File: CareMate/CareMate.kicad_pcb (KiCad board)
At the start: 2 copper layers, 88.9 x 76.2 mm, 24 parts, among them J1 Barrel_Jack_MountingPin, J2 Conn_01x16, J3 Conn_01x03, J4 Conn_01x03, J5 Conn_01x06, J6 Conn_01x03, J7 Servo, J9 Conn_01x16, U1 L7805, U2 LM386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

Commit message: fixed unconnected items
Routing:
- net GND: track 9.79 -> 35.2 mm, vias 1 -> 7
- added copper zone on B.Cu, net GND
- removed copper zone on B.Cu, net (none)
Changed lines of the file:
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@@
     (thickness 1.6)
     (drawings 10)
-    (tracks 240)
+    (tracks 258)
     (zones 0)
     (modules 24)
@@
   )
   (setup
-    (last_trace_width 0.381)
+    (last_trace_width 0.635)
     (user_trace_width 0.254)
     (user_trace_width 0.381)
@@
     (solder_mask_min_width 0.25)
     (aux_axis_origin 0 0)
-    (visible_elements 7FFFF7FF)
+    (visible_elements 7FFFFFFF)
     (pcbplotparams
       (layerselection 0x010fc_ffffffff)
@@
   (segment (start 123.952 27.686) (end 124.46 27.178) (width 0.381) (layer F.Cu) (net 2))
   (segment (start 122.654 27.686) (end 123.952 27.686) (width 0.381) (layer F.Cu) (net 2))
+  (via (at 113.284 52.324) (size 0.8) (drill 0.4) (layers F.Cu B.Cu) (net 2))
+  (segment (start 111.252 51.308) (end 112.268 51.308) (width 0.25) (layer F.Cu) (net 2))
+  (segment (start 112.268 51.308) (end 113.284 52.324) (width 0.25) (layer F.Cu) (net 2))
+  (segment (start 111.873 53.735) (end 113.284 52.324) (width 0.25) (layer F.Cu) (net 2))
+  (segment (start 111.252 53.735) (end 111.873 53.735) (width 0.25) (layer F.Cu) (net 2))
+  (via (at 98.552 33.782) (size 0.8) (drill 0.4) (layers F.Cu B.Cu) (net 2))
+  (segment (start 106.172 33.878) (end 98.648 33.878) (width 0.25) (layer F.Cu) (net 2))
+  (segment (start 98.648 33.878) (end 98.552 33.782) (width 0.25) (layer F.Cu) (net 2))
+  (via (at 62.484 41.402) (size 0.8) (drill 0.4) (layers F.Cu B.Cu) (net 2))
+  (segment (start 57.59 41.42) (end 62.466 41.42) (width 0.25) (layer F.Cu) (net 2))
+  (segment (start 62.466 41.42) (end 62.484 41.402) (width 0.25) (layer F.Cu) (net 2))
+  (via (at 54.102 67.056) (size 0.8) (drill 0.4) (layers F.Cu B.Cu) (net 2))
+  (segment (start 54.102 67.08) (end 54.102 67.056) (width 0.25) (layer B.Cu) (net 2))
+  (segment (start 50.292 70.89) (end 54.102 67.08) (width 0.25) (layer B.Cu) (net 2))
+  (via (at 133.096 39.624) (size 0.8) (drill 0.4) (layers F.Cu B.Cu) (net 2))
+  (via (at 134.112 44.704) (size 0.8) (drill 0.4) (layers F.Cu B.Cu) (net 2))
+  (segment (start 133.374 43.966) (end 134.112 44.704) (width 0.635) (layer B.Cu) (net 2))
+  (segment (start 132.08 43.966) (end 133.374 43.966) (width 0.635) (layer B.Cu) (net 2))
   (segment (start 111.111 55.626) (end 111.252 55.485) (width 0.381) (layer F.Cu) (net 3))
   (segment (start 106.172 55.626) (end 111.111 55.626) (width 0.381) (layer F.Cu) (net 3))
@@
   (segment (start 93.016 76.962) (end 92.964 77.014) (width 0.381) (layer F.Cu) (net 13))
   (segment (start 99.06 76.962) (end 93.016 76.962) (width 0.381) (layer F.Cu) (net 13))
-  (segment (start 67.362 51.816) (end 67.564 51.614) (width 0.381) (layer F.Cu) (net 22))
   (via (at 89.916 54.356) (size 0.8) (drill 0.4) (layers F.Cu B.Cu) (net 14))
   (segment (start 92.646 92.27) (end 89.916 89.54) (width 0.381) (layer B.Cu) (net 14))
@@
   (segment (start 66.899658 68.326) (end 67.201157 68.024501) (width 0.381) (layer F.Cu) (net 21))
   (segment (start 64.77 68.326) (end 66.899658 68.326) (width 0.381) (layer F.Cu) (net 21))
+  (segment (start 67.362 51.816) (end 67.564 51.614) (width 0.381) (layer F.Cu) (net 22))
   (via (at 50.038 52.07) (size 0.8) (drill 0.4) (layers F.Cu B.Cu) (net 22))
   (segment (start 67.564 51.614) (end 50.494 51.614) (width 0.381) (layer F.Cu) (net 22))
@@
   (segment (start 59.499188 49.82) (end 59.923689 50.244501) (width 0.381) (layer F.Cu) (net 37))
   (segment (start 57.59 49.82) (end 59.499188 49.82) (width 0.381) (layer F.Cu) (net 37))
-  (zone (net 0) (net_name "") (layer B.Cu) (hatch edge 0.508)
-    (connect_pads yes (clearance 0.508))
+  (zone (net 2) (net_name GND) (layer B.Cu) (hatch edge 0.508)
+    (connect_pads (clearance 0.508))
     (min_thickness 0.254)
     (fill yes (arc_segments 32) (thermal_gap 0.508) (thermal_bridge_width 0.508))

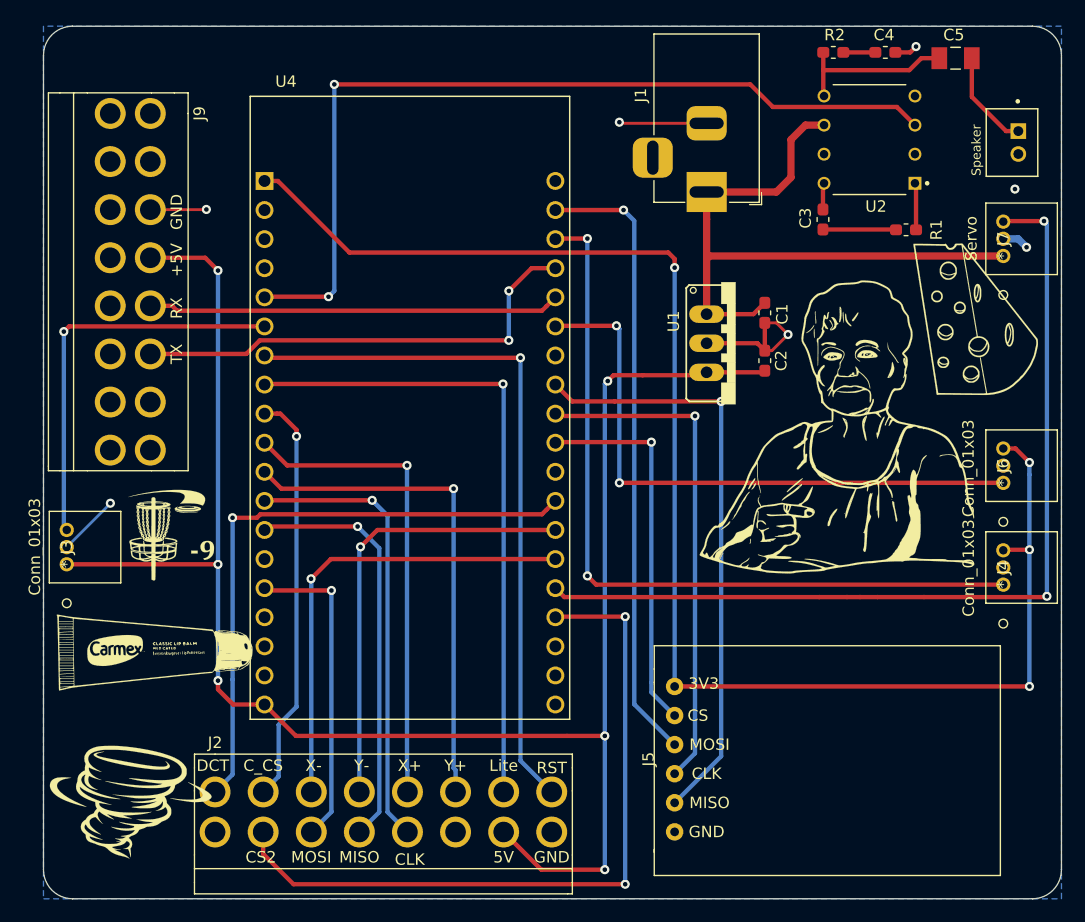
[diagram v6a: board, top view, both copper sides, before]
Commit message: added drill holes
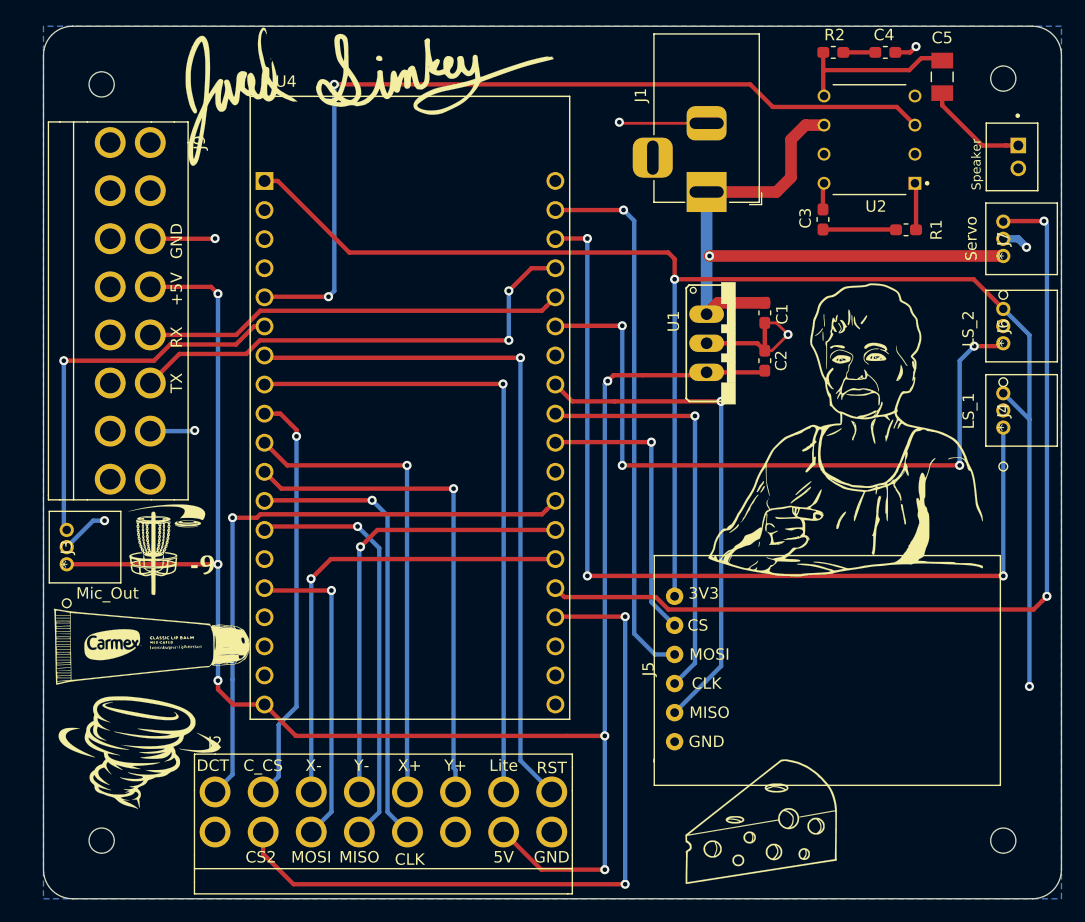
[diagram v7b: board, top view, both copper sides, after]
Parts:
- added G***: LOGO, MRDT_Silkscreens:z_sig_Jared_Sinkey_15.5mmx34.4mm, F.Cu at (77.0, 31.0)
- added REF**: MountingHole_2.2mm_M2_DIN965, MountingHole:MountingHole_2.2mm_M2_DIN965, F.Cu at (53.3, 30.5)
- added REF**: MountingHole_2.2mm_M2_DIN965, MountingHole:MountingHole_2.2mm_M2_DIN965, F.Cu at (132.1, 30.0)
- added REF**: MountingHole_2.2mm_M2_DIN965, MountingHole:MountingHole_2.2mm_M2_DIN965, F.Cu at (53.3, 96.5)
- added REF**: MountingHole_2.2mm_M2_DIN965, MountingHole:MountingHole_2.2mm_M2_DIN965, F.Cu at (132.1, 96.5)
- J3: value Conn_01x03 -> Mic_Out
- J4: value Conn_01x03 -> LS_1
- J6: value Conn_01x03 -> LS_2
- moved G*** 47.8 mm to (111.0, 95.2), turned to 0 degrees
- moved J4 13.7 mm to (132.1, 60.5)
- moved J6 12.2 mm to (132.1, 53.1)
- moved J5 7.87 mm to (103.4, 81.5)
- moved G*** 4.38 mm to (56.6, 88.9)
- moved J9 2.54 mm to (59.7, 35.6)
- moved C5 2.00 mm to (126.7, 29.8), turned to 90 degrees
- moved G*** 1.27 mm to (58.7, 71.1)
- moved Speaker 1.25 mm to (132.8, 36.8)
- moved G*** 0.80 mm to (114.0, 60.5)
- moved G*** 0.57 mm to (57.4, 79.8)
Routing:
- net LS_1: track 68.9 -> 81.6 mm, vias 2 -> 3
- net LS_2: track 52.7 -> 61.1 mm, vias 2 -> 4
- net MISO1: track 51.8 -> 43.9 mm
- net CS1: track 33.1 -> 25.2 mm
- net clk1: track 44.3 -> 36.4 mm
- net MOSI1: track 54.5 -> 47.6 mm
- net GND: track 35.2 -> 38.7 mm
- net 3.3V: track 131.6 -> 135.0 mm, vias 4 -> 2
- net +5V: track 158.7 -> 156.4 mm
- net Mic_Out: track 35.4 -> 33.9 mm
- net Tx_VoiceRec: track 41.0 -> 42.1 mm
- net Servo_1: track 79.7 -> 80.7 mm
- net Rx_VoiceRec: track 36.0 -> 36.7 mm
- net +9V: track 56.8 -> 56.4 mm, vias 0 -> 1

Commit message: PCB second revision
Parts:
- removed the G*** at (77.0, 31.0)
- removed J9: Conn_01x16, Additional Libraries:16PinConnector
- removed REF** (x4): MountingHole_2.2mm_M2_DIN965, MountingHole:MountingHole_2.2mm_M2_DIN965
- removed Speaker: Conn_01x02, Additional Libraries:JST_B2B-PH-K-S(LF)(SN)
- added Button 1: Molex_SL_02, Additional Libraries:Easy_2Pin, F.Cu at (52.8, 36.1)
- added Button 2: Molex_SL_02, Additional Libraries:Easy_2Pin, F.Cu at (52.9, 42.7)
- added J8: Conn_01x02, Additional Libraries:Easy_2Pin, F.Cu at (134.1, 33.5)
- J3: value Mic_Out -> Conn_01x03; footprint Additional Libraries:3PinConnector_Official -> Additional Libraries:Easy_3Pin
- J4: value LS_1 -> Conn_01x03; footprint Additional Libraries:3PinConnector_Official -> Additional Libraries:Easy_3Pin
- J6: value LS_2 -> Conn_01x03; footprint Additional Libraries:3PinConnector_Official -> Additional Libraries:Easy_3Pin
- J7: value Servo -> Conn_01x03; footprint Additional Libraries:3PinConnector_Official -> Additional Libraries:Easy_3Pin
- moved G*** 62.4 mm to (58.4, 61.7)
- moved G*** 48.5 mm to (57.9, 31.2)
- moved G*** 26.4 mm to (59.4, 44.7)
- moved J3 3.97 mm to (53.3, 69.8), turned to 0 degrees
- moved J7 3.88 mm to (134.1, 48.8), turned to 180 degrees
- moved G*** 2.30 mm to (56.4, 86.6)
- moved J6 1.93 mm to (132.8, 51.3), turned to 0 degrees
- moved J4 1.27 mm to (132.8, 61.5), turned to 0 degrees
- moved G*** 0.80 mm to (113.8, 59.7)
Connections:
- U4 pad 23: Tx_VoiceRec -> Button_1
- U4 pad 24: Rx_VoiceRec -> Button_2
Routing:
- net Button_1: track 0.00 -> 59.4 mm, vias 0 -> 3
- net Tx_VoiceRec: track 42.1 -> 0.00 mm, vias 2 -> 0
- net Button_2: track 0.00 -> 40.9 mm
- net Rx_VoiceRec: track 36.7 -> 0.00 mm
- net +5V: track 156.4 -> 123.6 mm, vias 6 -> 5
- net GND: track 38.7 -> 26.3 mm, vias 7 -> 4
- net Mic_Out: track 33.9 -> 42.7 mm
- net LS_2: track 61.1 -> 65.1 mm
- net LS_1: track 81.6 -> 85.4 mm
- net clk1: track 36.4 -> 39.9 mm
- net Y-: track 39.1 -> 35.5 mm
- net X-: track 40.7 -> 37.1 mm
- net MOSI1: track 47.6 -> 51.2 mm
- net MISO1: track 43.9 -> 47.5 mm
- net Card_Detect: track 53.4 -> 49.8 mm
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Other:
- board text added: "3.3V"
- board text added: "5V"
- board text added: "GND"
- board text added: "Mic Out"
- board text added: "Output"
- board text added: "Signal"
